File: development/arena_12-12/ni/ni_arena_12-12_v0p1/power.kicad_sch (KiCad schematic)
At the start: 5 parts, among them J1 Barrel_Jack, SW1 SW_SPDT, U6 AP2112K-3.3

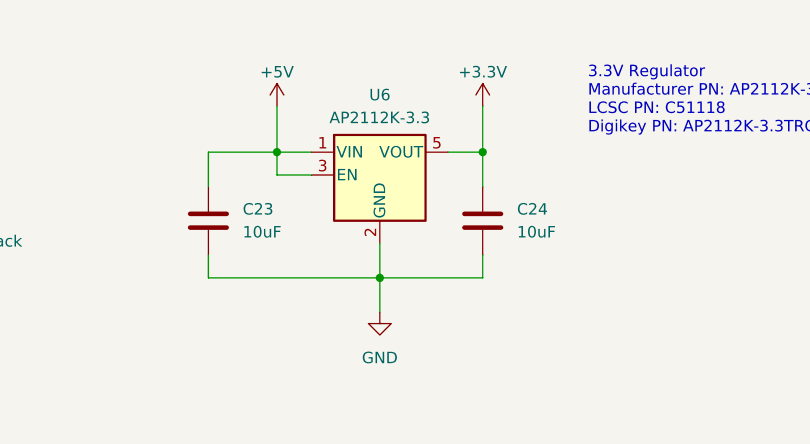
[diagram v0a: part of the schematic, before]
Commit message: Worked on schematic adding series termination resistors and buffers.
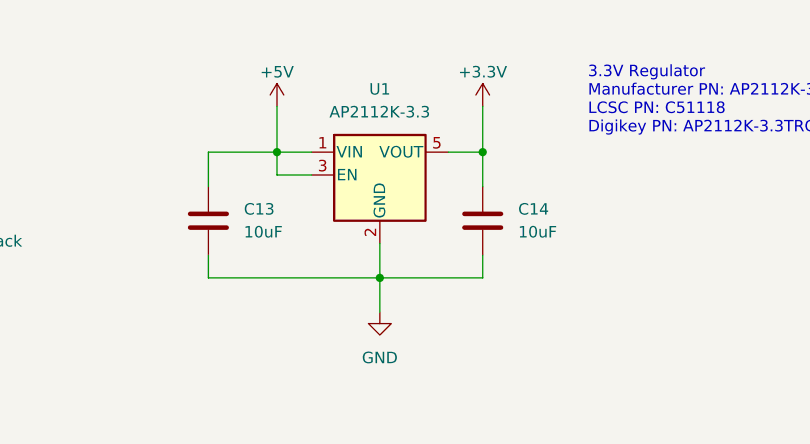
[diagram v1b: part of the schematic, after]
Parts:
- renumbered C23 to C13, C24 to C14, U6 to U1

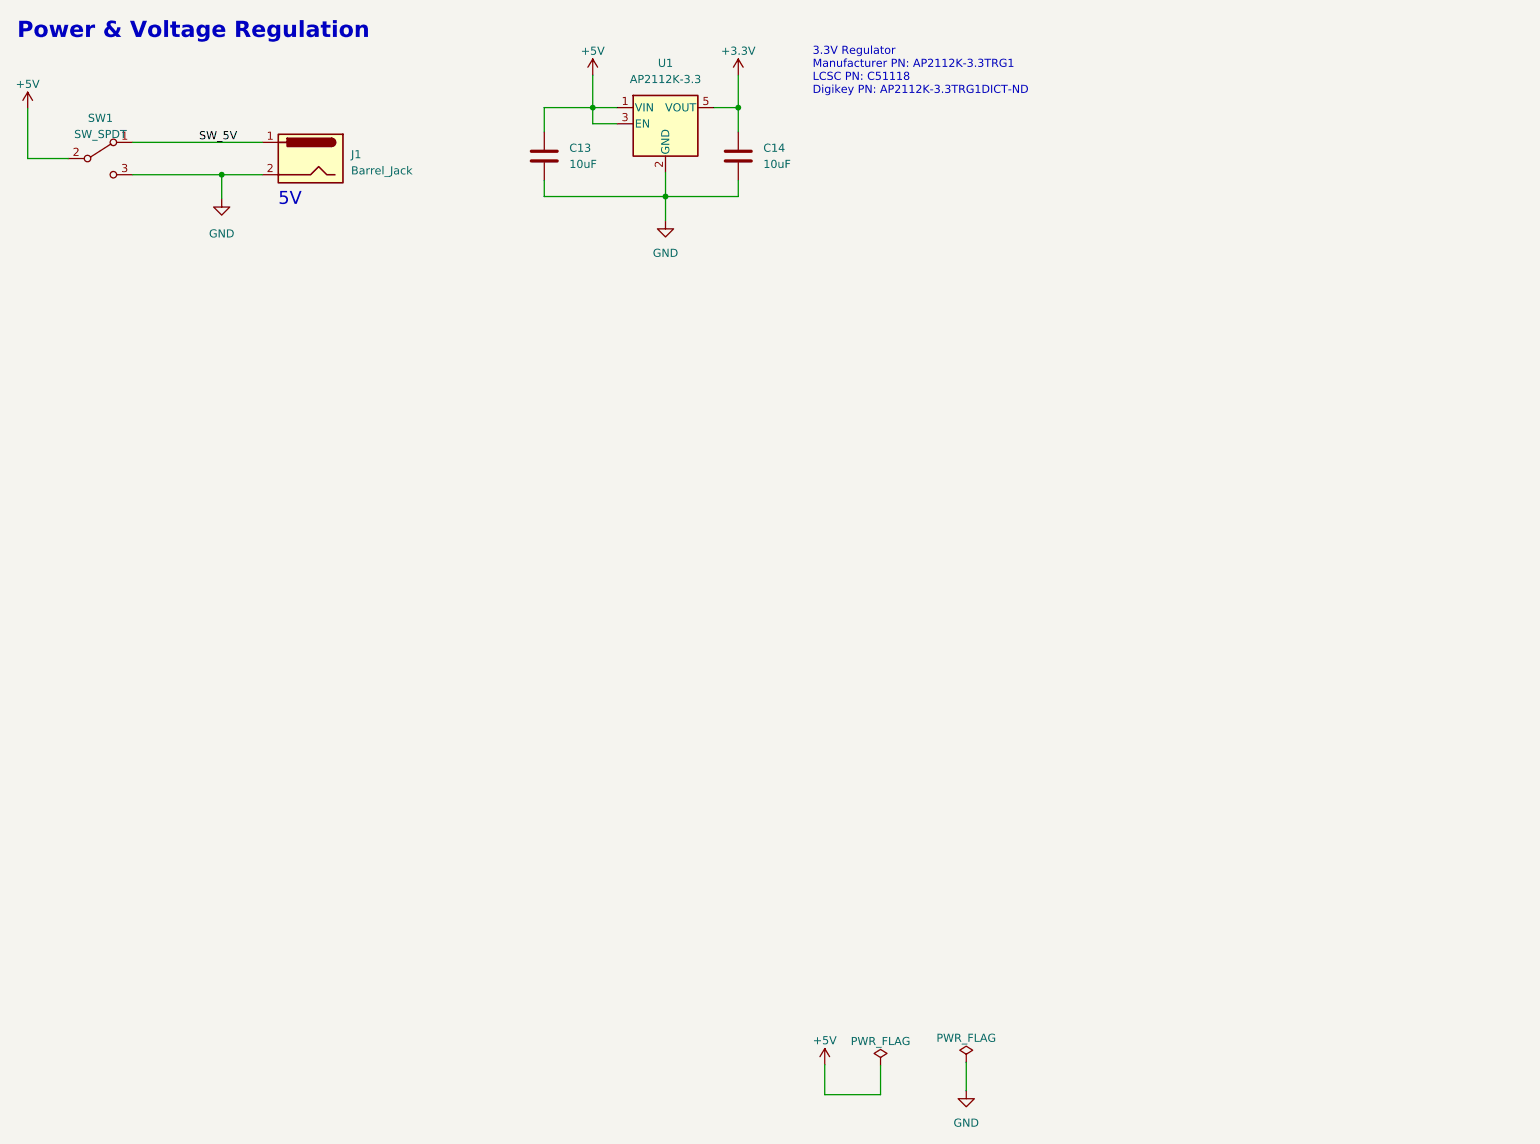
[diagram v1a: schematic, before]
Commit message: Finished initial schematic for 12-12 NI with schmitt buffers.
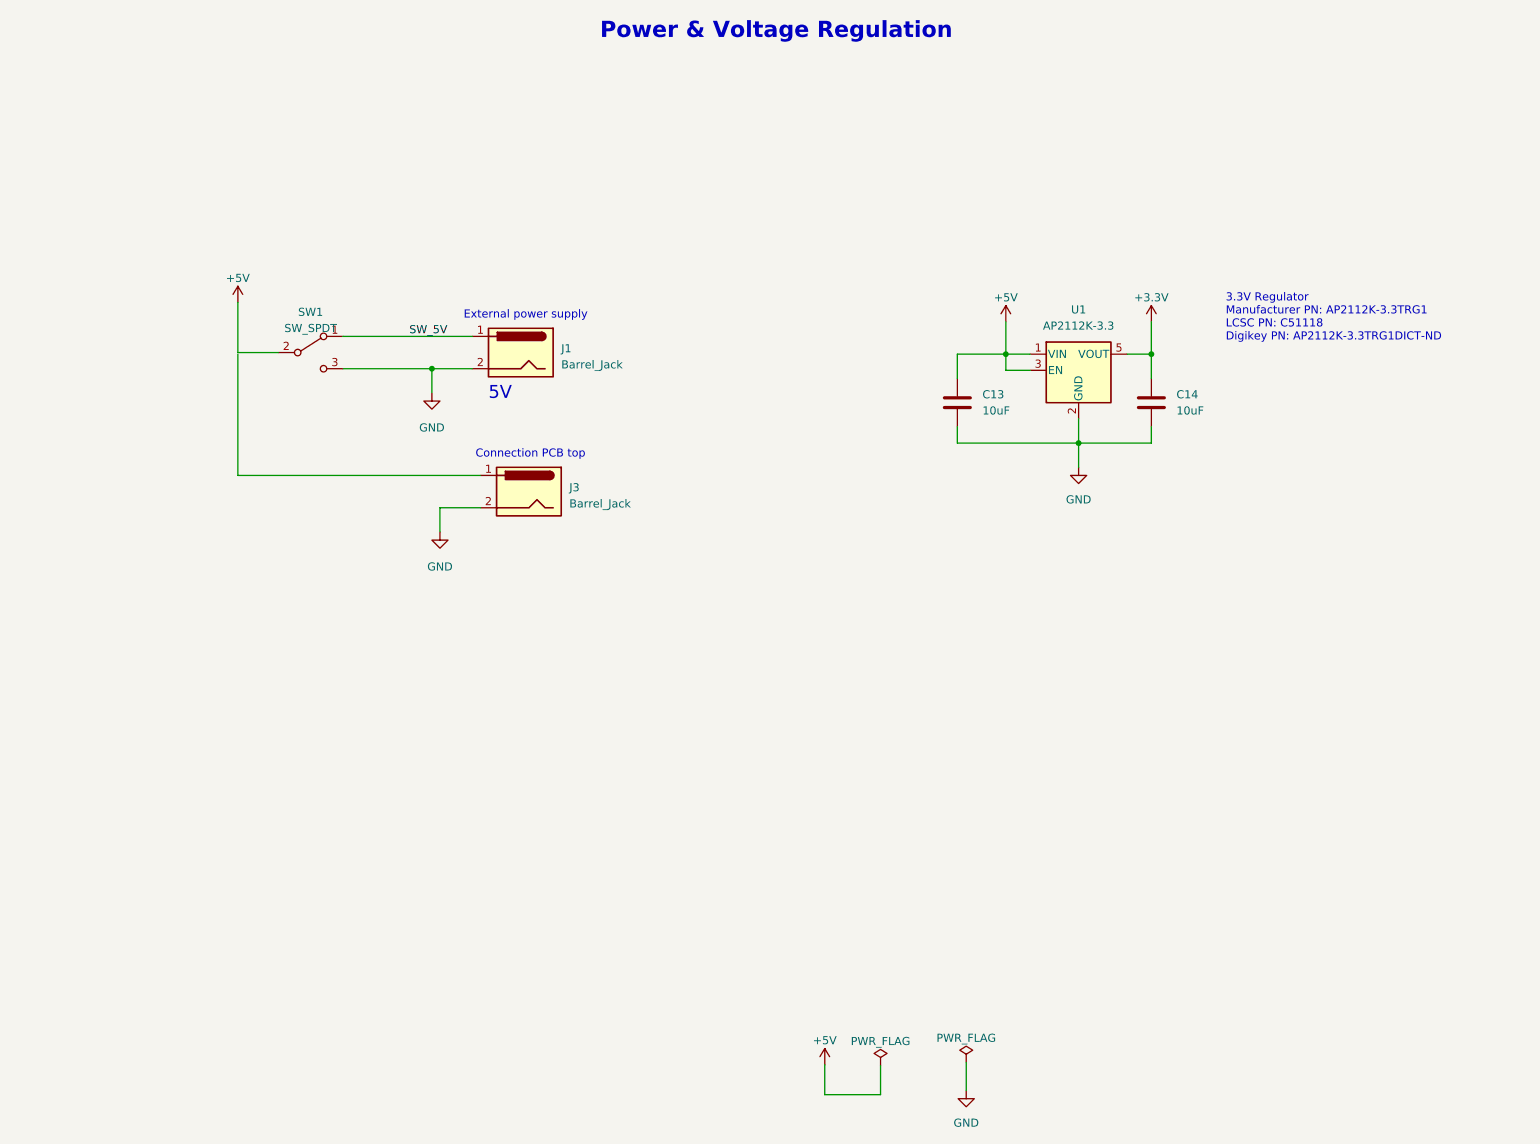
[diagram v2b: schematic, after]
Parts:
- added J3: Barrel_Jack, arena_custom:DCJACK_2PIN_HIGHCURRENT, symbol Connector:Barrel_Jack
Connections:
- net GND: now also J3.2
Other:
- note added: "Connection PCB top"
- note added: "External power supply"
- moved on the sheet: C13, C14, J1, SW1, U1

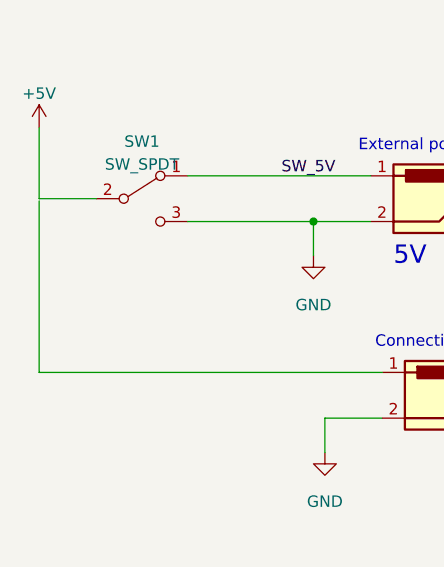
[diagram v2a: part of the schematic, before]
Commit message: ERC for NI 12-12 arena with schmitt buffers now passing.
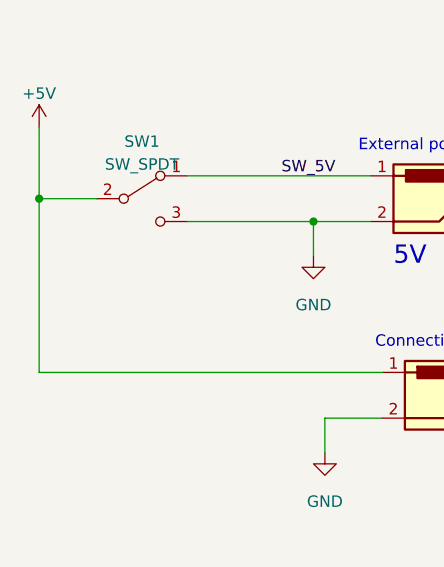
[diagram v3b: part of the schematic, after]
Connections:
- net +5V: now also J3.1
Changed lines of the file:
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@@
+	)
+	(junction
+		(at 54.61 69.596)
+		(diameter 0)
+		(color 0 0 0 0)
 	)
 	(junction
@@
 	(wire
 		(pts
+			(xy 54.61 69.596) (xy 54.61 88.9)
+		)
+		(stroke
+			(width 0)
+			(type default)
+		)
+	)
+	(wire
+		(pts
 			(xy 175.26 64.77) (xy 175.26 69.85)
 		)
@@
 		)
 		(stroke
-			(width 0)
-			(type default)
-		)
-	)
-	(wire
-		(pts
-			(xy 54.61 69.85) (xy 54.61 88.9)
-		)
-		(stroke

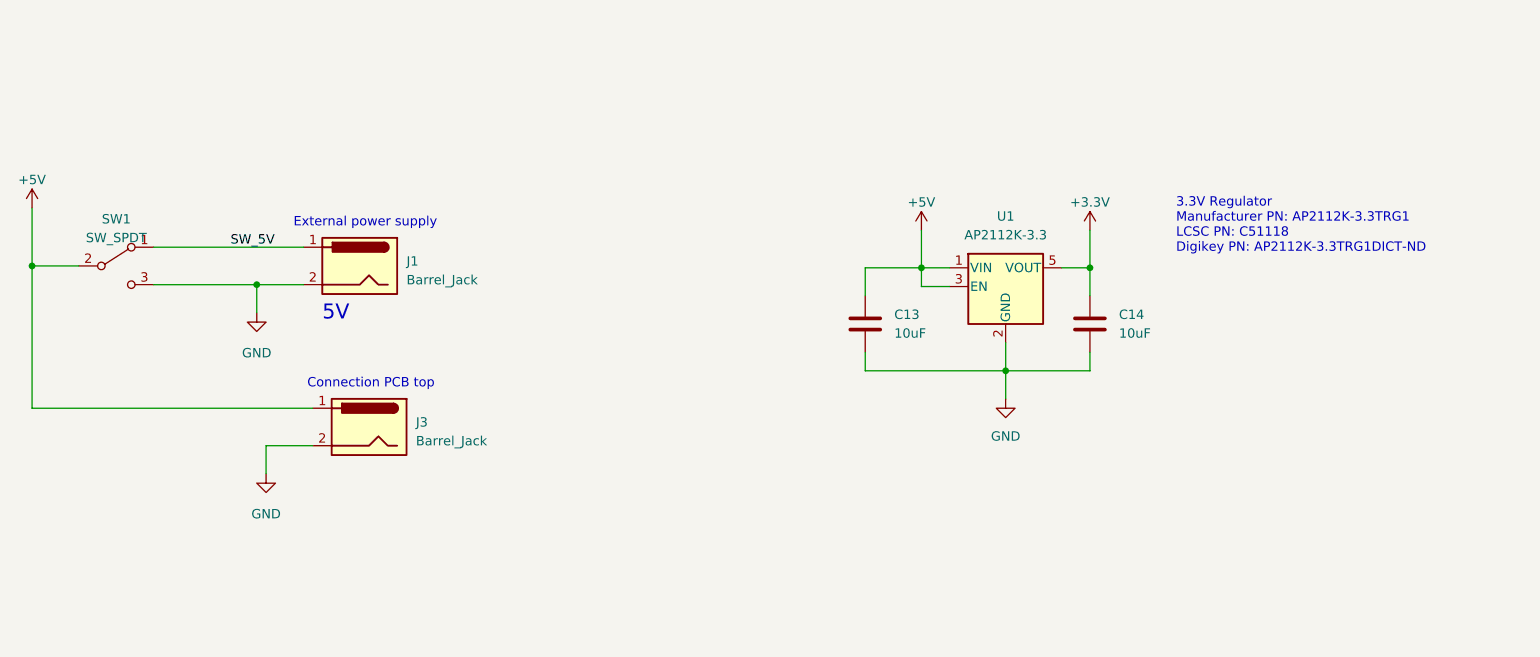
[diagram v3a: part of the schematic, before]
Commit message: Worked on 12-12 NI arena with schmitt buffers.
Finished footprint assignments.
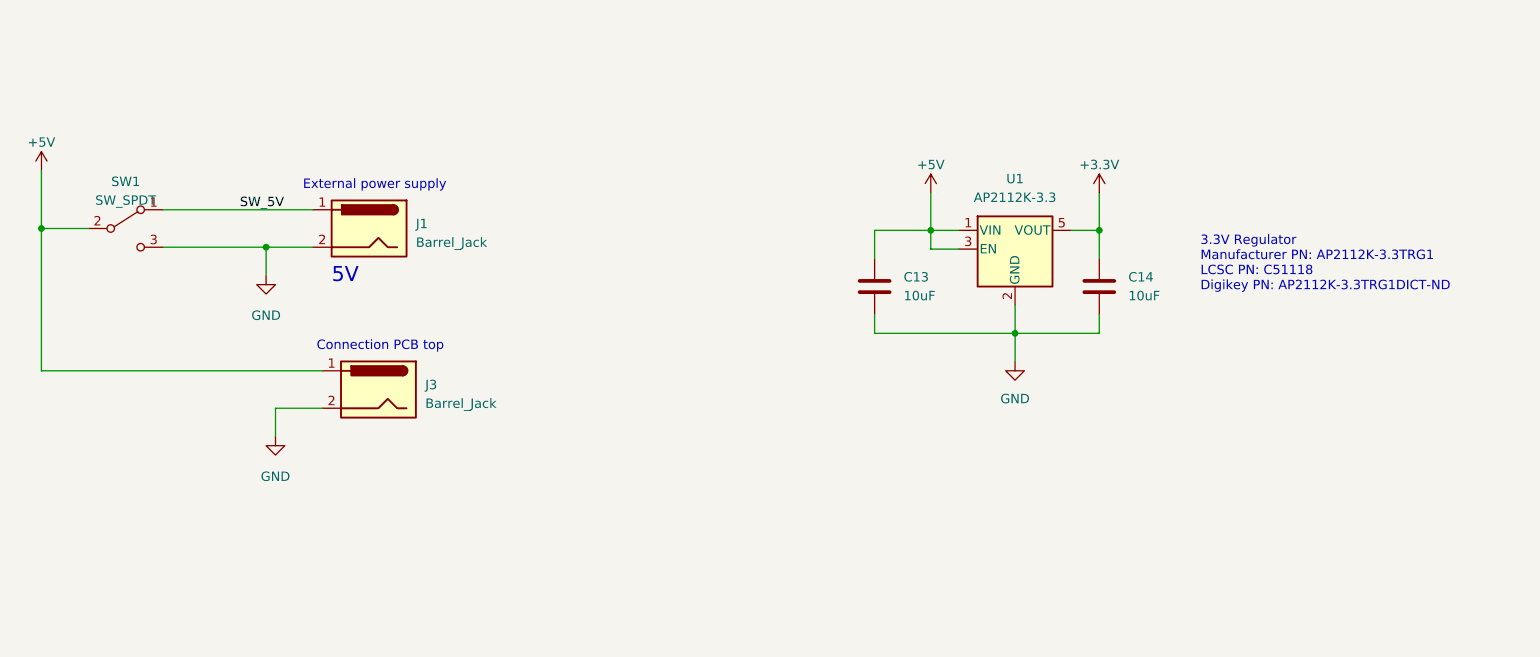
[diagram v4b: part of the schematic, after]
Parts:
- C13, C14: footprint Capacitor_SMD:C_0603_1608Metric -> Capacitor_SMD:C_1206_3216Metric
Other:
- moved on the sheet: C13, C14, J1, J3, SW1, U1
